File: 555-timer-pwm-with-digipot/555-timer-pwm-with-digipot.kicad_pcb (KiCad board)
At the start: 2 copper layers, 19 parts, among them J1 Conn_01x05_Pin

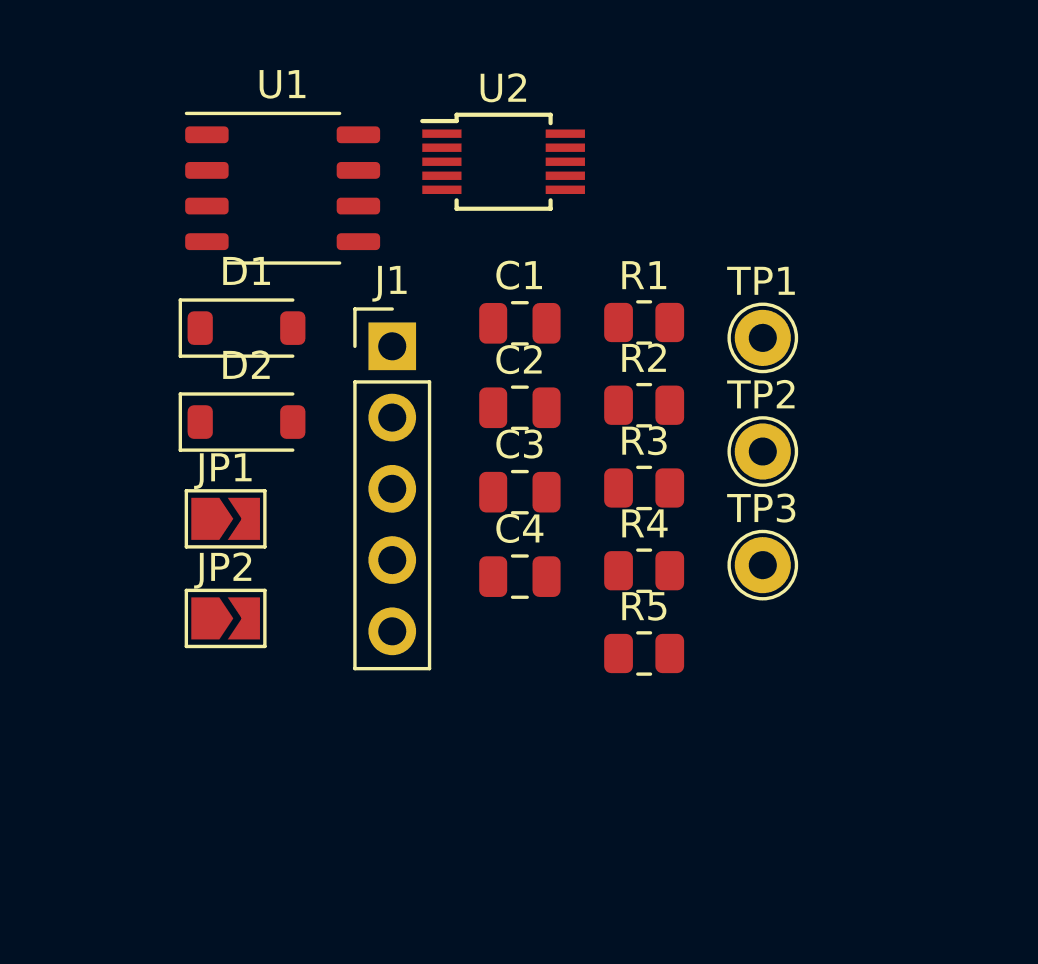
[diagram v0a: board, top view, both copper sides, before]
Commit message: Add completed first draft layout of 555-pwm pcb.
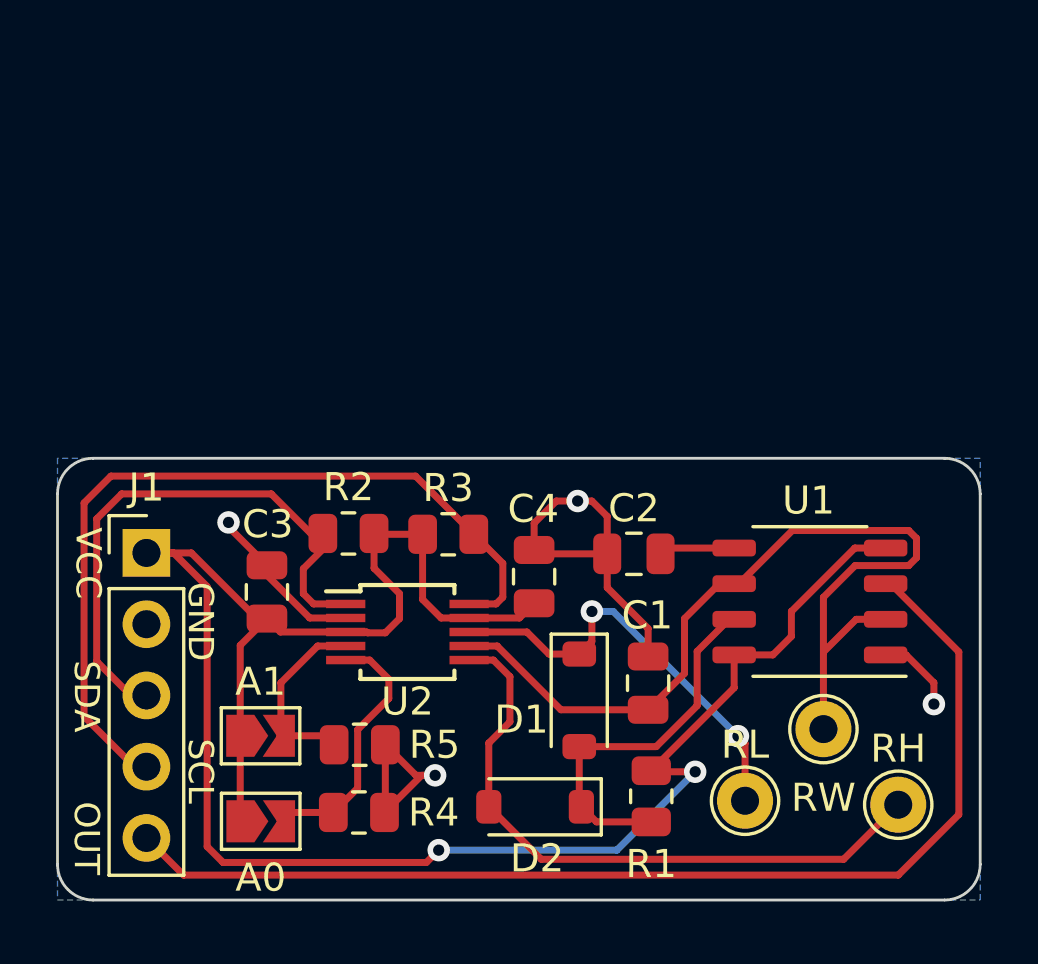
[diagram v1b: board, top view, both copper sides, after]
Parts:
- removed JP1, JP2: ~, Jumper:SolderJumper-2_P1.3mm_Open_TrianglePad1.0x1.5mm
- removed TP1, TP2, TP3: TestPoint, TestPoint:TestPoint_THTPad_D2.0mm_Drill1.0mm
- added A0: ~, Jumper:SolderJumper-2_P1.3mm_Open_TrianglePad1.0x1.5mm, F.Cu at (140.1, 97.5)
- added A1: ~, Jumper:SolderJumper-2_P1.3mm_Open_TrianglePad1.0x1.5mm, F.Cu at (140.1, 94.5)
- added RH: TestPoint, TestPoint:TestPoint_THTPad_D2.0mm_Drill1.0mm, F.Cu at (162.8, 96.9)
- added RL: TestPoint, TestPoint:TestPoint_THTPad_D2.0mm_Drill1.0mm, F.Cu at (157.4, 96.8)
- added RW: TestPoint, TestPoint:TestPoint_THTPad_D2.0mm_Drill1.0mm, F.Cu at (160.1, 94.2)
- moved U1 23.9 mm to (159.7, 89.7), turned to 180 degrees
- moved D1 17.8 mm to (151.4, 93.2), turned to -90 degrees
- moved D2 17.1 mm to (149.9, 97.0), turned to 180 degrees
- moved U2 17.1 mm to (145.3, 90.8)
- moved R1 16.9 mm to (154.0, 96.6), turned to -90 degrees
- moved C1 13.6 mm to (153.9, 92.6), turned to 90 degrees
- moved R4 13.3 mm to (143.6, 97.2)
- moved R2 11.5 mm to (143.2, 87.3), turned to 180 degrees
- moved J1 11.4 mm to (136.0, 88.0)
- moved R5 10.6 mm to (143.6, 94.8)
- moved C3 9.69 mm to (140.3, 89.3), turned to -90 degrees
- moved R3 7.18 mm to (146.8, 87.3)
- moved C2 6.61 mm to (153.4, 88.0), turned to 180 degrees
- moved C4 0.51 mm to (149.8, 88.8), turned to 90 degrees
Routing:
- net VCC: track 0.00 -> 75.3 mm, vias 0 -> 2
- net /out: track 0.00 -> 39.8 mm
- net Net-(U1-THRES): track 0.00 -> 32.8 mm
- net /scl: track 0.00 -> 29.7 mm
- net GND: track 0.00 -> 28.2 mm, vias 0 -> 4
- net Net-(D2-A): track 0.00 -> 22.8 mm
- net /sda: track 0.00 -> 20.5 mm
- net Net-(D1-K): track 0.00 -> 15.4 mm, vias 0 -> 2
- net Net-(D1-A): track 0.00 -> 13.4 mm
- net /a0: track 0.00 -> 9.38 mm
- net /a1: track 0.00 -> 6.77 mm
- net Net-(U1-CONT): track 0.00 -> 2.71 mm
- added copper zone on B.Cu, net GND
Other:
- board outline added: 32.9 x 15.7 mm
- board text added: "GND"
- board text added: "OUT"
- board text added: "SCL"
- board text added: "SDA"
- board text added: "VCC"

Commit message: Small changes to 555-timer pcb layout.
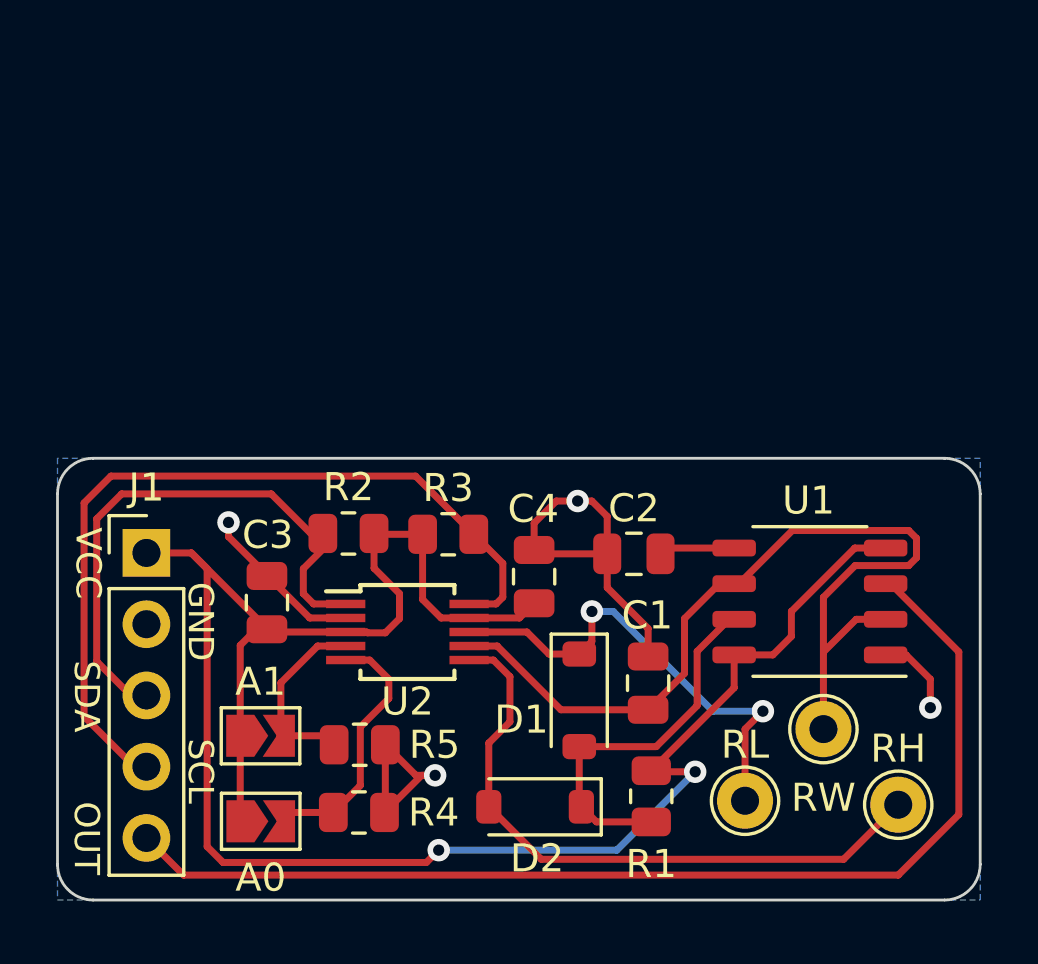
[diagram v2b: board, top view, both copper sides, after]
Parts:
- moved C3 0.38 mm to (140.3, 89.7)
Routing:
- net Net-(D1-K): track 15.4 -> 17.0 mm
- net VCC: track 75.3 -> 73.9 mm

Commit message: Small pcb layout changes to 555-timer pwm design.
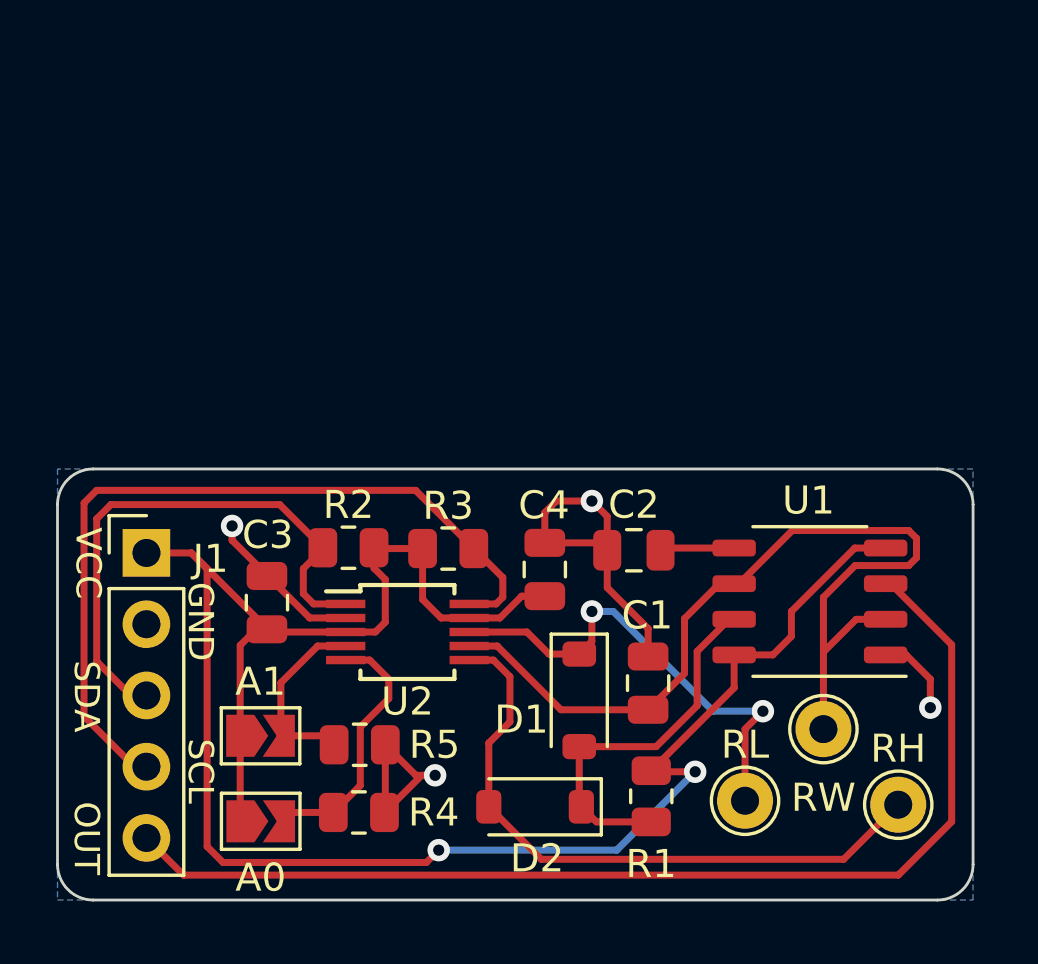
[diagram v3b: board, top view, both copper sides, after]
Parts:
- moved R2 0.51 mm to (143.2, 87.8)
- moved R3 0.51 mm to (146.8, 87.8)
- moved C4 0.46 mm to (150.2, 88.5)
- moved C2 0.13 mm to (153.4, 87.9)
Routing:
- net VCC: track 73.9 -> 72.7 mm
- net GND: track 28.2 -> 27.3 mm
- net /scl: track 29.7 -> 29.0 mm
- net /sda: track 20.5 -> 19.9 mm
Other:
- board size 32.9 x 15.7 mm -> 32.6 x 15.4 mm
